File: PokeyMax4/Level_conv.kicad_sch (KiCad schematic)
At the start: 4 parts, among them U2 SN74CB3T16211SM, U4 SN74CB3T16211SM

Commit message: Update the v4 board
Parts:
- U2, U4: JLCPCB Part # C2674751 -> (none); LCSC Part # (none) -> C2653275

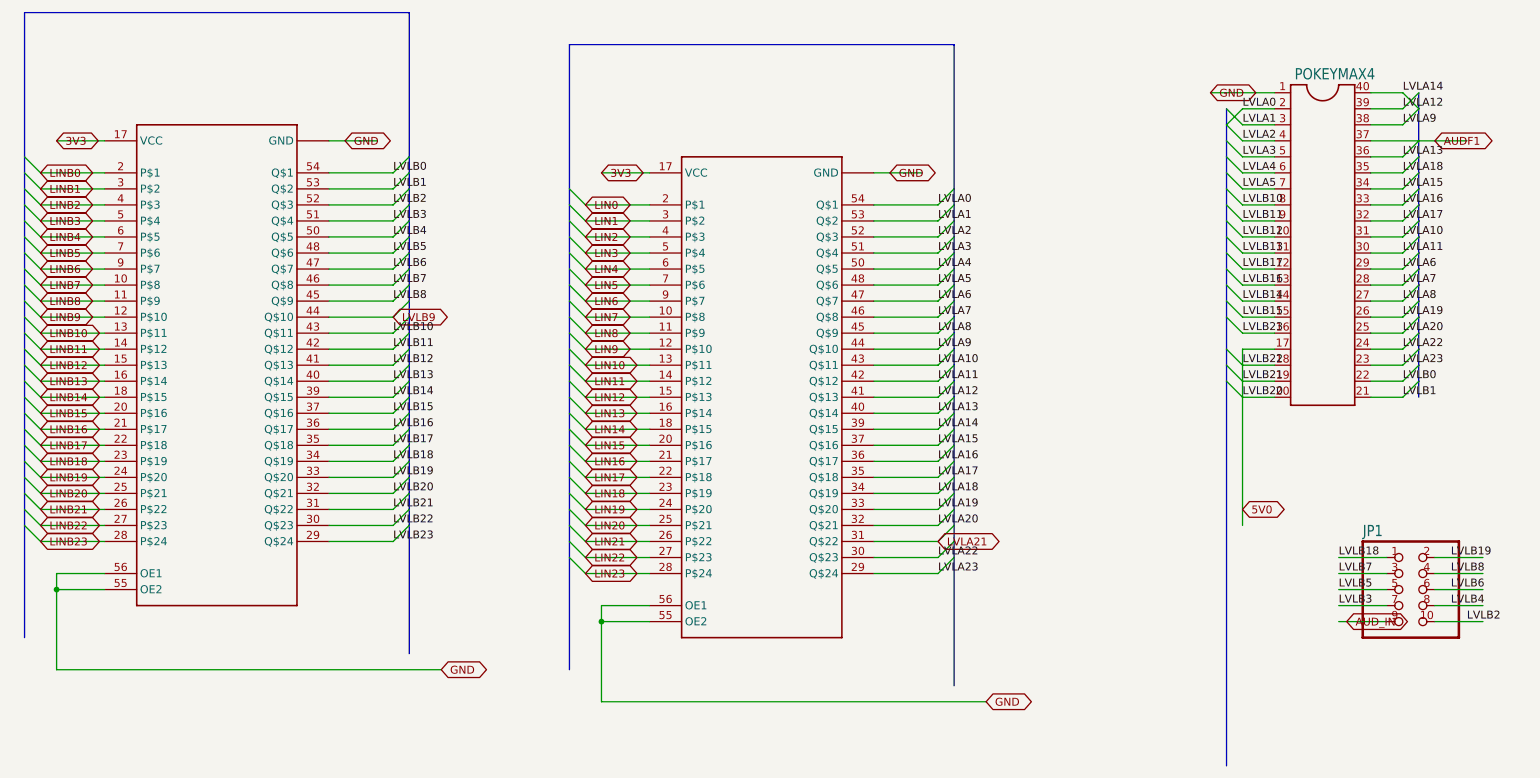
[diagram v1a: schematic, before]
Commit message: Updates for JLCPCB fabrication and parts library
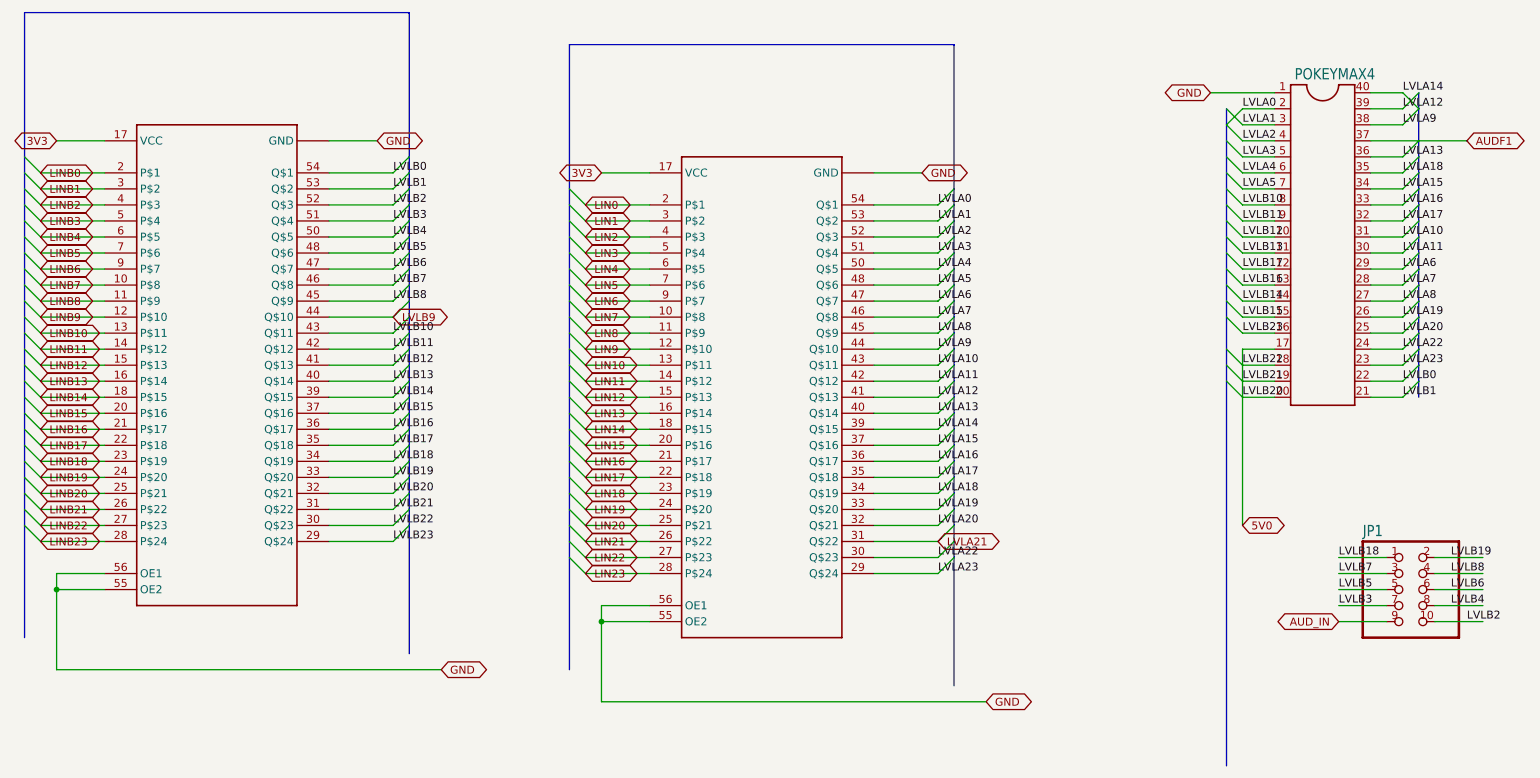
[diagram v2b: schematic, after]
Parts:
- JP1, POKEYMAX4: now left out of the parts list
- U2: JLCPCB Rotation Offset (none) -> 90; LCSC Part # C2653275 -> C2674751
- U4: JLCPCB Rotation Offset (none) -> 270; LCSC Part # C2653275 -> C2674751
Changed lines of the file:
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@@
 	(wire
 		(pts
-			(xy 246.38 139.7) (xy 238.76 139.7)
-		)
-		(stroke
-			(width 0.1524)
-			(type solid)
-		)
-	)
-	(wire
-		(pts
 			(xy 88.9 104.14) (xy 78.74 104.14)
 		)
@@
 	(wire
 		(pts
+			(xy 223.52 104.14) (xy 223.52 124.46)
+		)
+		(stroke
+			(width 0.1524)
+			(type solid)
+		)
+	)
+	(wire
+		(pts
 			(xy 248.92 60.96) (xy 243.84 60.96)
 		)
@@
 	(wire
 		(pts
+			(xy 238.76 139.7) (xy 246.38 139.7)
+		)
+		(stroke
+			(width 0.1524)
+			(type solid)
+		)
+	)
+	(wire
+		(pts
 			(xy 35.56 134.62) (xy 43.18 134.62)
 		)
@@
 	(wire
 		(pts
-			(xy 223.52 104.14) (xy 223.52 124.46)
-		)
-		(stroke
-			(width 0.1524)
-			(type solid)
-		)
-	)
-	(wire
-		(pts
 			(xy 228.6 96.52) (xy 223.52 96.52)
 		)
@@
 	(global_label "GND"
 		(shape bidirectional)
-		(at 218.44 55.88 0)
+		(at 218.44 55.88 180)
 		(fields_autoplaced yes)
 		(effects
@@
 				(size 1.2446 1.2446)
 			)
-			(justify left)
+			(justify right)
 		)
 		(property "Intersheetrefs" "${INTERSHEET_REFS}"
@@
 	(global_label "AUD_IN"
 		(shape bidirectional)
-		(at 240.03 139.7 0)
+		(at 238.76 139.7 180)
 		(fields_autoplaced yes)
 		(effects
@@
 				(size 1.2446 1.2446)
 			)
-			(justify left)
+			(justify right)
 		)
 		(property "Intersheetrefs" "${INTERSHEET_REFS}"
-			(at 250.5044 139.7 0)
+			(at 249.2344 139.7 0)
 			(effects
 				(font
@@
 	(global_label "3V3"
 		(shape bidirectional)
-		(at 35.56 63.5 0)
+		(at 35.56 63.5 180)
 		(fields_autoplaced yes)
 		(effects
@@
 				(size 1.2446 1.2446)
 			)
-			(justify left)
+			(justify right)
 		)
 		(property "Intersheetrefs" "${INTERSHEET_REFS}"
@@
 	(global_label "AUDF1"
 		(shape bidirectional)
-		(at 254 63.5 0)
+		(at 259.08 63.5 0)
 		(fields_autoplaced yes)
 		(effects
@@
 		)
 		(property "Intersheetrefs" "${INTERSHEET_REFS}"
-			(at 263.8816 63.5 0)
+			(at 268.9616 63.5 0)
 			(effects
 				(font
@@
 	(global_label "5V0"
 		(shape bidirectional)
-		(at 223.52 121.92 0)
+		(at 223.52 124.46 0)
 		(fields_autoplaced yes)
 		(effects
@@
 		)
 		(property "Intersheetrefs" "${INTERSHEET_REFS}"
-			(at 230.9716 121.92 0)
+			(at 230.9716 124.46 0)
 			(effects
 				(font
@@
 	(global_label "GND"
 		(shape bidirectional)
-		(at 81.28 63.5 0)
+		(at 86.36 63.5 0)
 		(fields_autoplaced yes)
 		(effects
@@
 		)
 		(property "Intersheetrefs" "${INTERSHEET_REFS}"
-			(at 89.0873 63.5 0)
+			(at 94.1673 63.5 0)
 			(effects
 				(font
@@
 	(global_label "GND"
 		(shape bidirectional)
-		(at 167.64 68.58 0)
+		(at 172.72 68.58 0)
 		(fields_autoplaced yes)
 		(effects
@@
 		)
 		(property "Intersheetrefs" "${INTERSHEET_REFS}"
-			(at 175.4473 68.58 0)
+			(at 180.5273 68.58 0)
 			(effects
 				(font
@@
 	(global_label "3V3"
 		(shape bidirectional)
-		(at 121.92 68.58 0)
+		(at 121.92 68.58 180)
 		(fields_autoplaced yes)
 		(effects
@@
 				(size 1.2446 1.2446)
 			)
-			(justify left)
+			(justify right)
 		)
 		(property "Intersheetrefs" "${INTERSHEET_REFS}"
@@
 			)
 		)
-		(property "LCSC Part #" "C2653275"
+		(property "LCSC Part #" "C2674751"
+			(at 154.94 99.06 0)
+			(effects
+				(font
+					(size 1.27 1.27)
+				)
+				(hide yes)
+			)
+		)
+		(property "JLCPCB Rotation Offset" "90"
 			(at 154.94 99.06 0)
 			(effects
@@
 		(unit 1)
 		(exclude_from_sim no)
-		(in_bom yes)
+		(in_bom no)
 		(on_board yes)
 		(dnp no)
@@
 			)
 		)
+		(property "JLCPCB Rotation Offset" ""
+			(at 248.92 134.62 0)
+			(effects
+				(font
+					(size 1.27 1.27)
+				)
+				(hide yes)
+			)
+		)
 		(pin "1"
 		)
@@
 			)
 		)
-		(property "LCSC Part #" "C2653275"
+		(property "LCSC Part #" "C2674751"
+			(at 68.58 93.98 0)
+			(effects
+				(font
+					(size 1.27 1.27)
+				)
+				(hide yes)
+			)
+		)
+		(property "JLCPCB Rotation Offset" "270"
 			(at 68.58 93.98 0)
 			(effects
@@
 		(unit 1)
 		(exclude_from_sim no)
-		(in_bom yes)
+		(in_bom no)
 		(on_board yes)
 		(dnp no)
@@
 			(at 236.22 78.74 0)
 			(effects
+				(font
+					(size 1.27 1.27)
+				)
+				(hide yes)
+			)
+		)
+		(property "JLCPCB Rotation Offset" ""
+			(at 236.22 78.74 0)
+			(effects

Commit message: Final adjustements to production files for JLC
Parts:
- U2: JLCPCB Rotation Offset 90 -> 270
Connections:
- net 5V0: no longer POKEYMAX4.18, POKEYMAX4.19, POKEYMAX4.20, U4.30 (Q$23), U4.31 (Q$22), U4.32 (Q$21)
- new net LVLB20: POKEYMAX4.20, U4.32 (Q$21)
- new net LVLB21: POKEYMAX4.19, U4.31 (Q$22)
- new net LVLB22: POKEYMAX4.18, U4.30 (Q$23)
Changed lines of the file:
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@@
 	(wire
 		(pts
-			(xy 243.84 63.5) (xy 251.46 63.5)
-		)
-		(stroke
-			(width 0.1524)
-			(type solid)
-		)
-	)
-	(wire
-		(pts
 			(xy 238.76 132.08) (xy 246.38 132.08)
 		)
@@
 		)
 	)
-	(wire
-		(pts
-			(xy 223.52 99.06) (xy 223.52 101.6)
-		)
-		(stroke
-			(width 0.1524)
-			(type solid)
-		)
-	)
 	(bus
 		(pts
@@
 	(wire
 		(pts
-			(xy 223.52 104.14) (xy 223.52 124.46)
-		)
-		(stroke
-			(width 0.1524)
-			(type solid)
-		)
-	)
-	(wire
-		(pts
 			(xy 248.92 60.96) (xy 243.84 60.96)
 		)
@@
 		)
 	)
-	(wire
-		(pts
-			(xy 223.52 96.52) (xy 223.52 99.06)
-		)
-		(stroke
-			(width 0.1524)
-			(type solid)
-		)
-	)
 	(bus
 		(pts
@@
 		)
 	)
-	(wire
-		(pts
-			(xy 223.52 101.6) (xy 223.52 104.14)
-		)
-		(stroke
-			(width 0.1524)
-			(type solid)
-		)
-	)
 	(bus
 		(pts
@@
 	(wire
 		(pts
-			(xy 228.6 96.52) (xy 223.52 96.52)
-		)
-		(stroke
-			(width 0.1524)
-			(type solid)
-		)
-	)
-	(wire
-		(pts
 			(xy 33.02 68.58) (xy 43.18 68.58)
 		)
@@
 	(wire
 		(pts
-			(xy 251.46 63.5) (xy 259.08 63.5)
-		)
-		(stroke
-			(width 0.1524)
-			(type solid)
-		)
-	)
-	(wire
-		(pts
 			(xy 88.9 119.38) (xy 78.74 119.38)
 		)
@@
 	(wire
 		(pts
-			(xy 228.6 55.88) (xy 218.44 55.88)
-		)
-		(stroke
-			(width 0.1524)
-			(type solid)
-		)
-	)
-	(wire
-		(pts
 			(xy 35.56 132.08) (xy 35.56 134.62)
 		)
@@
 	(global_label "GND"
 		(shape bidirectional)
-		(at 218.44 55.88 180)
+		(at 228.6 55.88 180)
 		(fields_autoplaced yes)
 		(effects
@@
 		)
 		(property "Intersheetrefs" "${INTERSHEET_REFS}"
-			(at 226.2473 55.88 0)
+			(at 236.4073 55.88 0)
 			(effects
 				(font
@@
 	(global_label "AUDF1"
 		(shape bidirectional)
-		(at 259.08 63.5 0)
+		(at 243.84 63.5 0)
 		(fields_autoplaced yes)
 		(effects
@@
 		)
 		(property "Intersheetrefs" "${INTERSHEET_REFS}"
-			(at 268.9616 63.5 0)
+			(at 253.7216 63.5 0)
 			(effects
 				(font
@@
 	(global_label "5V0"
 		(shape bidirectional)
-		(at 223.52 124.46 0)
+		(at 228.6 96.52 180)
 		(fields_autoplaced yes)
 		(effects
@@
 				(size 1.2446 1.2446)
 			)
-			(justify left)
+			(justify right)
 		)
 		(property "Intersheetrefs" "${INTERSHEET_REFS}"
-			(at 230.9716 124.46 0)
+			(at 221.1484 96.52 0)
 			(effects
 				(font
 					(size 1.27 1.27)
 				)
-				(justify left)
+				(justify right)
 				(hide yes)
 			)
@@
 			)
 		)
-		(property "JLCPCB Rotation Offset" "90"
+		(property "JLCPCB Rotation Offset" "270"
 			(at 154.94 99.06 0)
 			(effects
